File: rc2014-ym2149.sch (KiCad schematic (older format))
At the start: 29 parts, among them J1 AUDIO OUT, J2 IO Out, P1 RC2014 BUS, U1 74HCT138, U2 74HCT138, U3 74HCT00, U4 74HCT74, U5 AY-3-8190/YM2149F

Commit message: Modified schematic to support MSX-compatible ports
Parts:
- added JP?: USE !A3 FOR ENABLE, rc2014:Pin_Header_Straight_1x03_Pitch2.54mm, symbol Jumper_Dual
- JP2: value ENABLE SELECTOR -> SEPARATE READ PORT
- JP4: symbol CONN_02X08 -> CONN_02X09
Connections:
- net labels added: /CS
- net labels removed: CS
- wire segments 217 -> 251
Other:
- moved on the sheet: JP1, JP2, JP3, JP7, U3C

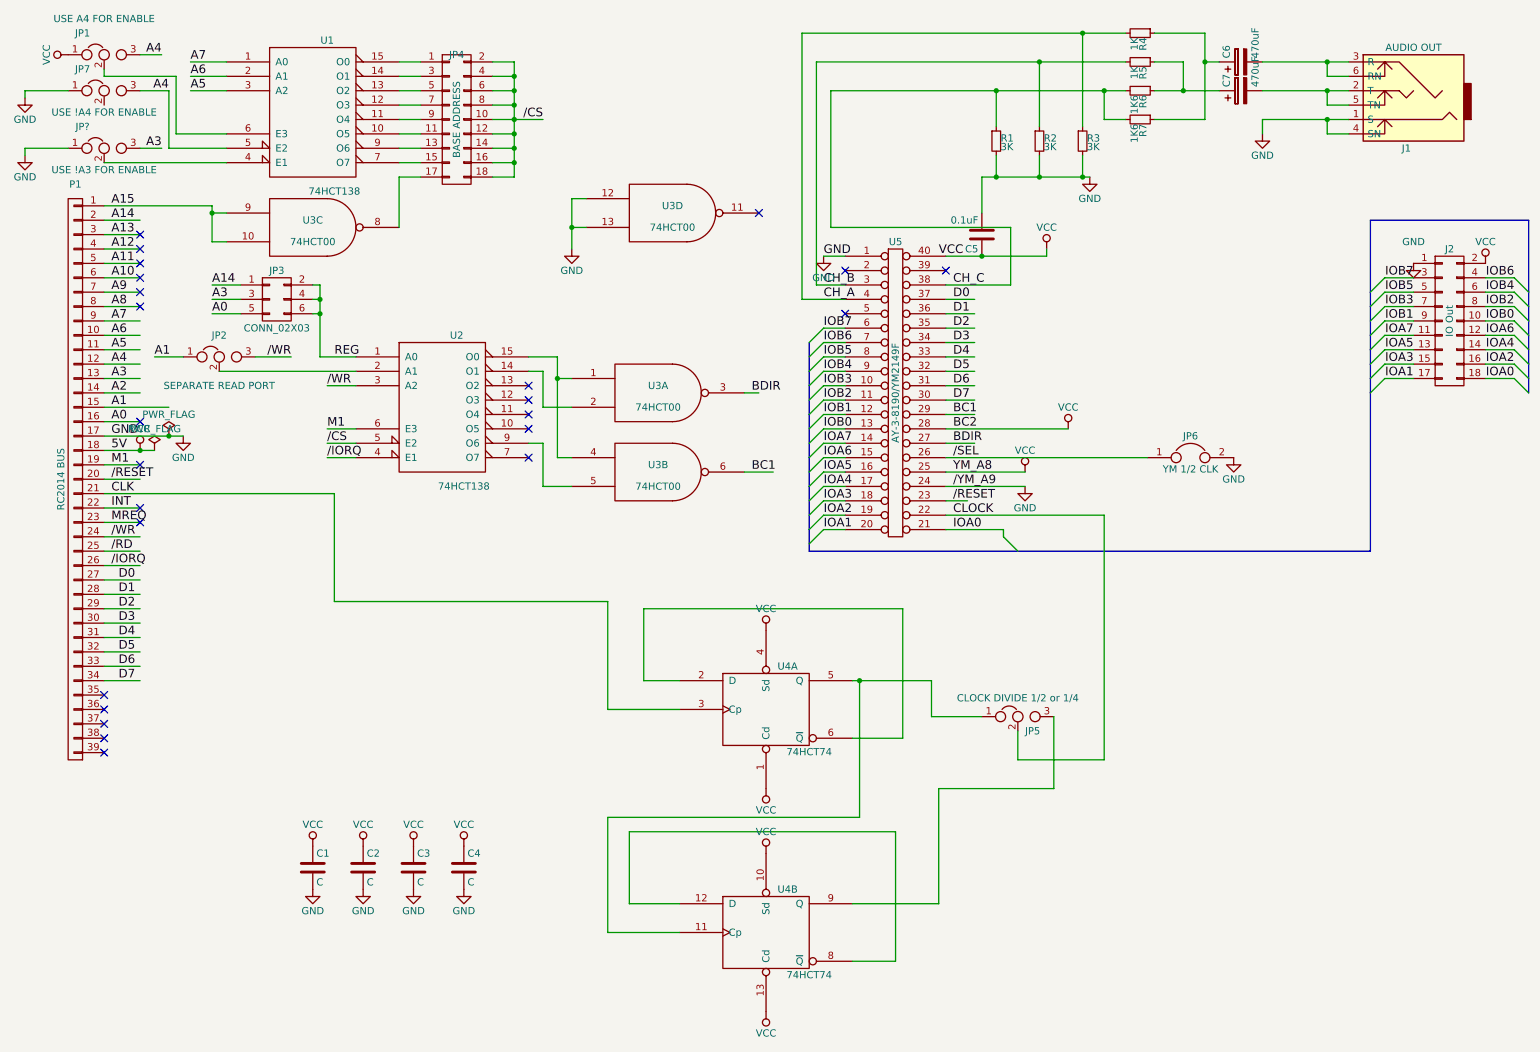
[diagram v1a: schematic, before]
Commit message: Modifications to schematic - now passes ERC
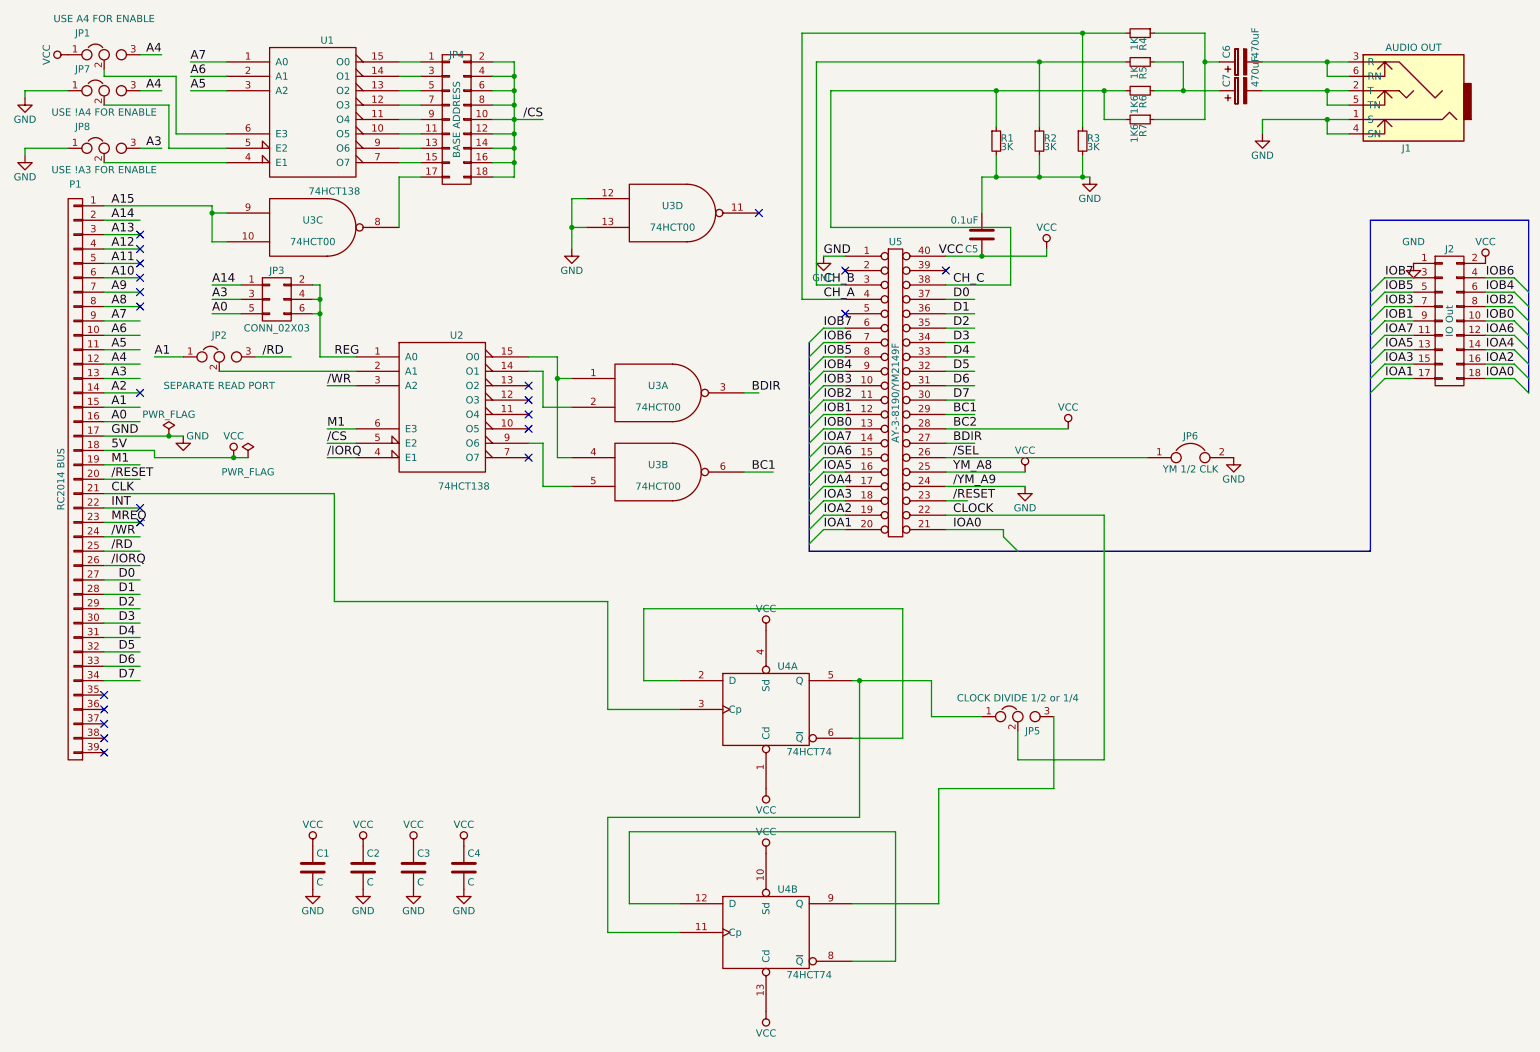
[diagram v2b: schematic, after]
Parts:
- gave numbers to parts that had none: 1
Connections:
- wire segments 251 -> 225
- no-connect marks 24 -> 23
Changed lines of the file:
@@
 Sheet 1 1
 Title "RC2014 YM2149 / AY-3-8910 sound card"
-Date "2017-07-16"
-Rev "5"
+Date "2018-07-09"
+Rev "pre-6"
 Comp ""
 Comment1 ""
@@
 P 1650 3400
 F 0 "#PWR01" H 1650 3150 50  0001 C CNN
-F 1 "GND" H 1650 3250 50  0000 C CNN
+F 1 "GND" H 1750 3400 50  0000 C CNN
 F 2 "" H 1650 3400 50  0000 C CNN
 F 3 "" H 1650 3400 50  0000 C CNN
@@
 L VCC #PWR02
 U 1 1 5898D2A5
-P 1350 3500
-F 0 "#PWR02" H 1350 3350 50  0001 C CNN
-F 1 "VCC" H 1350 3650 50  0000 C CNN
-F 2 "" H 1350 3500 50  0000 C CNN
-F 3 "" H 1350 3500 50  0000 C CNN
-	1    1350 3500
+P 2000 3550
+F 0 "#PWR02" H 2000 3400 50  0001 C CNN
+F 1 "VCC" H 2000 3700 50  0000 C CNN
+F 2 "" H 2000 3550 50  0000 C CNN
+F 3 "" H 2000 3550 50  0000 C CNN
+	1    2000 3550
 	1    0    0    -1
 $EndComp
@@
 Text Label 2650 3450 0    60   ~ 0
 /CS
-Text Label 2400 2850 2    60   ~ 0
-/WR
 $Comp
 L CONN_02X03 JP3
@@
 	1    0    0    -1
 $EndComp
-Text Label 1550 1000 2    60   ~ 0
+Text Label 1500 1000 2    60   ~ 0
 A4
 $Comp
@@
 L PWR_FLAG #FLG029
 U 1 1 58E0EDBF
-P 1450 3500
-F 0 "#FLG029" H 1450 3575 50  0001 C CNN
-F 1 "PWR_FLAG" H 1450 3650 50  0000 C CNN
-F 2 "" H 1450 3500 50  0001 C CNN
-F 3 "" H 1450 3500 50  0001 C CNN
-	1    1450 3500
+P 2100 3550
+F 0 "#FLG029" H 2100 3625 50  0001 C CNN
+F 1 "PWR_FLAG" H 2100 3450 50  0000 C CNN
+F 2 "" H 2100 3550 50  0001 C CNN
+F 3 "" H 2100 3550 50  0001 C CNN
+	1    2100 3550
 	1    0    0    -1
 $EndComp
@@
 NoConn ~ 1350 3900
 NoConn ~ 1350 4000
-NoConn ~ 1350 3600
-NoConn ~ 1350 3300
+NoConn ~ 1350 3100
 NoConn ~ 1350 2500
 NoConn ~ 1350 2400
@@
 /WR
 $Comp
-L Jumper_Dual JP?
+L Jumper_Dual JP8
 U 1 1 5B29E934
 P 1100 1400
-F 0 "JP?" H 950 1550 50  0000 C CNN
+F 0 "JP8" H 950 1550 50  0000 C CNN
 F 1 "USE !A3 FOR ENABLE" H 1100 1250 50  0000 C CNN
 F 2 "rc2014:Pin_Header_Straight_1x03_Pitch2.54mm" H 1100 200 50  0001 C CNN
@@
 $EndComp
 $Comp
-L GND #PWR?
+L GND #PWR030
 U 1 1 5B29EC80
 P 550 1450
-F 0 "#PWR?" H 550 1200 50  0001 C CNN
+F 0 "#PWR030" H 550 1200 50  0001 C CNN
 F 1 "GND" H 550 1300 50  0000 C CNN
 F 2 "" H 550 1450 50  0001 C CNN
@@
 	1100 3300 1350 3300
 Wire Wire Line
-	1100 3400 1550 3400
-Wire Wire Line
-	1550 3400 1650 3400
-Wire Wire Line
-	1100 3500 1350 3500
-Wire Wire Line
-	1350 3500 1450 3500
+	1100 3400 1650 3400
+Wire Wire Line
+	1450 3550 2100 3550
 Wire Wire Line
 	1100 3700 1350 3700
@@
 	6250 4050 6100 4050
 Wire Wire Line
-	6950 2150 7200 2150
-Wire Wire Line
-	7200 2150 7650 2150
+	6950 2150 7650 2150
 Wire Wire Line
 	6950 2350 7400 2350
@@
 	6300 6650 6900 6650
 Wire Bus Line
-	6000 2750 6000 2850
+	6000 2750 6000 4200
 Wire Bus Line
-	6000 2850 6000 2950
-Wire Bus Line
-	6000 2950 6000 3050
-Wire Bus Line
-	6000 3050 6000 3150
-Wire Bus Line
-	6000 3150 6000 3250
-Wire Bus Line
-	6000 3250 6000 3350
-Wire Bus Line
-	6000 3350 6000 3450
-Wire Bus Line
-	6000 3450 6000 3550
-Wire Bus Line
-	6000 3550 6000 3650
-Wire Bus Line
-	6000 3650 6000 3750
-Wire Bus Line
-	6000 3750 6000 3850
-Wire Bus Line
-	6000 3850 6000 3950
-Wire Bus Line
-	6000 3950 6000 4050
-Wire Bus Line
-	6000 4050 6000 4150
-Wire Bus Line
-	6000 4150 6000 4200
-Wire Bus Line
-	6000 4200 7450 4200
-Wire Bus Line
-	7450 4200 9900 4200
+	9900 4200 6000 4200
 Wire Wire Line
 	10700 3000 10900 3000
@@
 	7350 4050 7350 4100
 Wire Wire Line
-	9150 1000 9600 1000
-Wire Wire Line
-	9600 1000 9750 1000
-Wire Wire Line
-	9150 800  9600 800
-Wire Wire Line
-	9600 800  9750 800
-Wire Wire Line
-	9150 1200 9600 1200
-Wire Wire Line
-	9600 1200 9750 1200
+	9150 1000 9750 1000
+Wire Wire Line
+	9150 800  9750 800
+Wire Wire Line
+	9150 1200 9750 1200
 Wire Wire Line
 	9150 1200 9150 1300
@@
 	7400 1950 6150 1950
 Wire Wire Line
-	6150 1000 7300 1000
-Wire Wire Line
-	7300 1000 8050 1000
-Wire Wire Line
-	8050 1000 8200 1000
+	6150 1000 8200 1000
 Wire Wire Line
 	8050 1200 8200 1200
@@
 	8400 600  8750 600
 Wire Wire Line
-	5950 600  7900 600
-Wire Wire Line
-	7900 600  8200 600
+	5950 600  8200 600
 Wire Wire Line
 	5950 600  5950 2450
 Wire Wire Line
-	6050 800  7600 800
-Wire Wire Line
-	7600 800  8200 800
+	6050 800  8200 800
 Wire Wire Line
 	6050 800  6050 2350
@@
 	7900 1600 7900 1450
 Wire Wire Line
-	7200 1600 7300 1600
-Wire Wire Line
-	7300 1600 7600 1600
-Wire Wire Line
-	7600 1600 7900 1600
-Wire Wire Line
-	7900 1600 7950 1600
+	7200 1600 7950 1600
 Connection ~ 7600 1600
 Wire Wire Line
 	7200 1850 7200 1600
 Wire Wire Line
-	8750 600  8750 800
-Wire Wire Line
-	8750 800  8750 1200
+	8750 600  8750 1200
 Wire Wire Line
 	8750 800  8850 800
@@
 	8600 800  8600 1000
 Wire Wire Line
-	8400 1000 8600 1000
-Wire Wire Line
-	8600 1000 8850 1000
+	8400 1000 8850 1000
 Connection ~ 8600 1000
 Connection ~ 8750 800
@@
 	6950 3450 7150 3450
 Wire Wire Line
-	1550 3200 1100 3200
+	1350 3200 1100 3200
 Wire Wire Line
 	1100 3600 1350 3600
@@
 	2550 2350 2600 2350
 Wire Wire Line
-	2600 2350 2600 2450
-Wire Wire Line
-	2600 2450 2600 2550
-Wire Wire Line
-	2600 2550 2600 2850
+	2600 2350 2600 2850
 Wire Wire Line
 	2550 2450 2600 2450
@@
 	3800 800  3950 800
 Wire Wire Line
-	3950 800  3950 900
-Wire Wire Line
-	3950 900  3950 1000
-Wire Wire Line
-	3950 1000 3950 1100
-Wire Wire Line
-	3950 1100 3950 1200
-Wire Wire Line
-	3950 1200 3950 1300
-Wire Wire Line
-	3950 1300 3950 1400
-Wire Wire Line
-	3950 1400 3950 1500
-Wire Wire Line
-	3950 1500 3950 1600
+	3950 800  3950 1600
 Wire Wire Line
 	3800 900  3950 900
@@
 	2150 2850 2400 2850
 Connection ~ 1550 3400
-Connection ~ 1350 3500
+Connection ~ 2000 3550
 Wire Wire Line
 	8050 5650 7450 5650
@@
 	7700 5850 7700 5350
 Wire Wire Line
-	6300 5100 6350 5100
-Wire Wire Line
-	6350 5100 6850 5100
+	6300 5100 6850 5100
 Wire Wire Line
 	6850 5100 6850 5350
@@
 	6850 5350 7200 5350
 Wire Wire Line
-	4350 1750 4350 1950
-Wire Wire Line
-	4350 1950 4350 2100
+	4350 1750 4350 2100
 Wire Wire Line
 	3950 1500 3800 1500
 Wire Bus Line
-	9900 4200 9900 3100
-Wire Bus Line
-	9900 3100 9900 3000
-Wire Bus Line
-	9900 3000 9900 2900
-Wire Bus Line
-	9900 2900 9900 2800
-Wire Bus Line
-	9900 2800 9900 2700
-Wire Bus Line
-	9900 2700 9900 2600
-Wire Bus Line
-	9900 2600 9900 2500
-Wire Bus Line
-	9900 2500 9900 2400
-Wire Bus Line
-	9900 2400 9900 1900
+	9900 1900 9900 4200
 Wire Bus Line
 	9900 1900 11000 1900
 Wire Bus Line
-	11000 1900 11000 2400
-Wire Bus Line
-	11000 2400 11000 2500
-Wire Bus Line
-	11000 2500 11000 2600
-Wire Bus Line
-	11000 2600 11000 2700
-Wire Bus Line
-	11000 2700 11000 2800
-Wire Bus Line
-	11000 2800 11000 2900
-Wire Bus Line
-	11000 2900 11000 3000
-Wire Bus Line
-	11000 3000 11000 3100
+	11000 1900 11000 3100
 Wire Wire Line
 	1100 1500 1950 1500
@@
 	1350 750  1500 750
 Wire Wire Line
-	1550 1000 1350 1000
+	1500 1000 1350 1000
 Wire Wire Line
 	850  1000 550  1000
@@
 	1600 900  1100 900
 Wire Wire Line
-	3800 1200 3950 1200
-Wire Wire Line
-	3950 1200 4150 1200
+	3800 1200 4150 1200
 Connection ~ 1850 1850
 Wire Wire Line
 	1850 2050 1950 2050
 Wire Wire Line
-	1850 1800 1850 1850
-Wire Wire Line
-	1850 1850 1850 2050
+	1850 1800 1850 2050
 Wire Wire Line
 	3150 1950 3150 1600
@@
 Wire Wire Line
 	1550 1400 1950 1400
-Wire Wire Line
-	1550 1000 1550 1400
 Wire Wire Line
 	850  1400 550  1400
@@
 	4050 2850 4250 2850
 Wire Wire Line
-	4250 2850 4250 3000
-Wire Wire Line
-	4250 3000 4250 3550
+	4250 2850 4250 3550
 Wire Wire Line
 	4250 3550 4350 3550
@@
 Wire Wire Line
 	4150 3450 4150 3750
+Wire Wire Line
+	1550 1400 1550 1100
+Wire Wire Line
+	1550 1100 1100 1100
+Text Label 2200 2850 0    60   ~ 0
+/RD
+Wire Wire Line
+	1450 3550 1450 3500
+Wire Wire Line
+	1450 3500 1100 3500
 $EndSCHEMATC
